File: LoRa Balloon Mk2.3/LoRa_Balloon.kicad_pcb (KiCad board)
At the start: 2 copper layers, 30 x 56 mm, 257 parts, among them J1 COAX, J2 Qwicc_6-pin, J3 Qwiic_4pin, U1 SKY67013-396LF_CID141, U2 SX1272IMLTRICT-ND_CID104, U3 SKY67013-396LF_CID141, U4 PE4259_CID105, U5 ATMEGA328P-AU, U6 XCL205, X1 X1E0000210162_CID142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

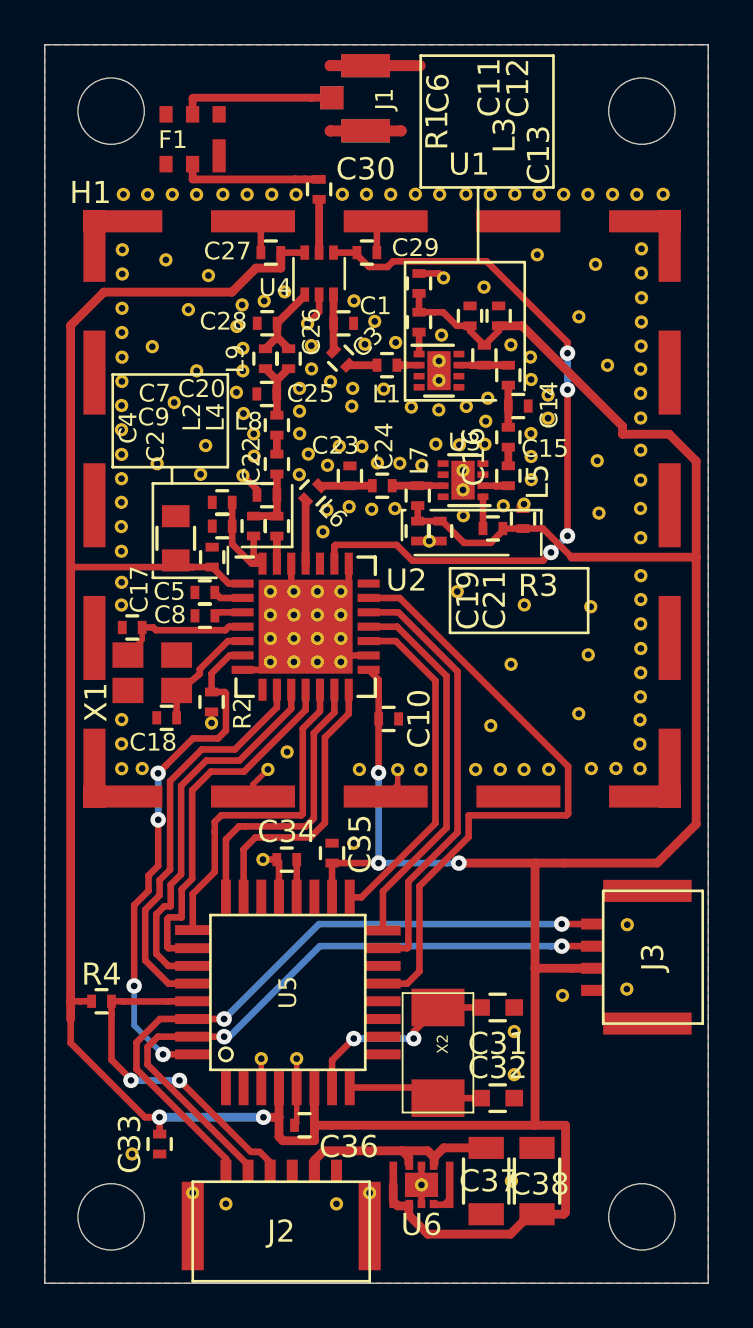
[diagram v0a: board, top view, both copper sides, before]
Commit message: Updated libraries
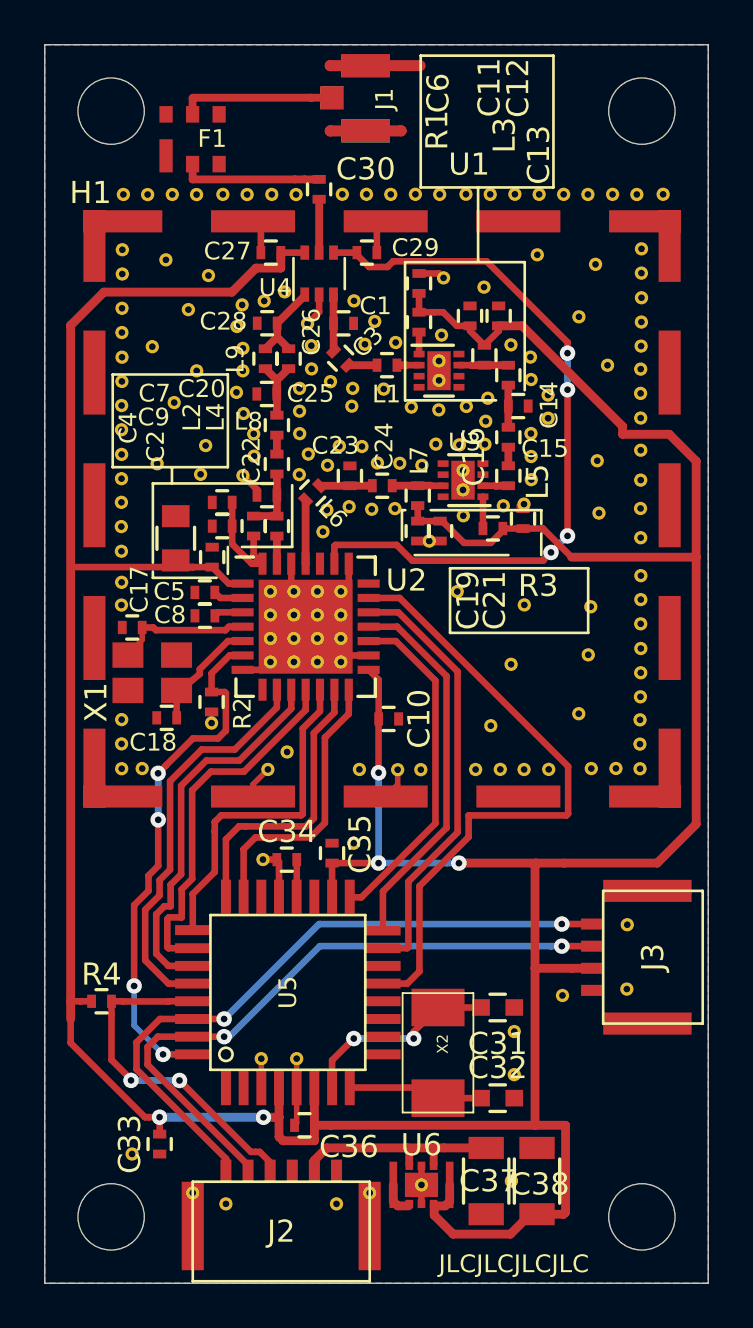
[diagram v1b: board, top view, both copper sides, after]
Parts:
- turned F1 to 0 degrees
- turned U6 to 0 degrees
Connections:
- U6 pad GND: (no net) -> GND
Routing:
- net +3V3: track 188.2 -> 187.1 mm
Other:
- board text added: "JLCJLCJLCJLC"
